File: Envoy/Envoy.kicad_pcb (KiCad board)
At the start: 2 copper layers, 95.4 x 95.4 mm, 57 parts

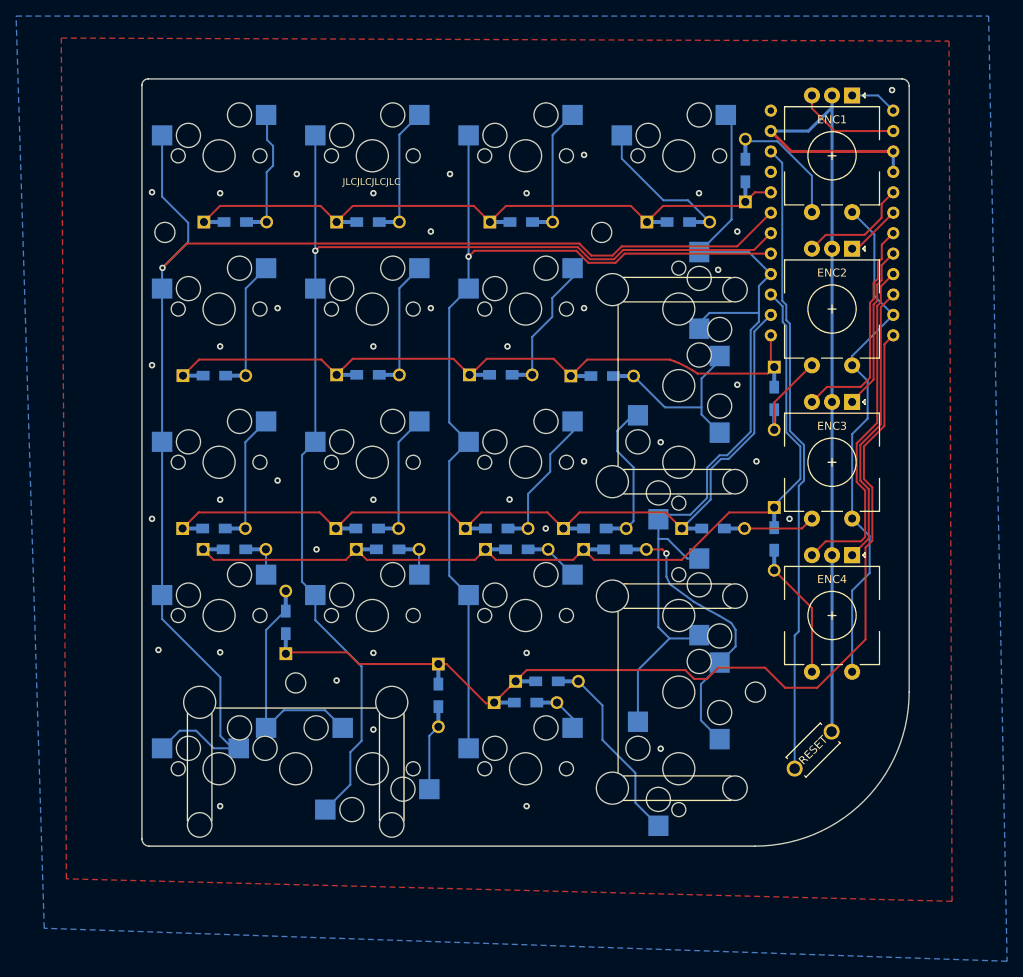
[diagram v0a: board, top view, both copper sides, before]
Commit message: curves!  Fun curved traces.  Prepare rev0.2 gerbers
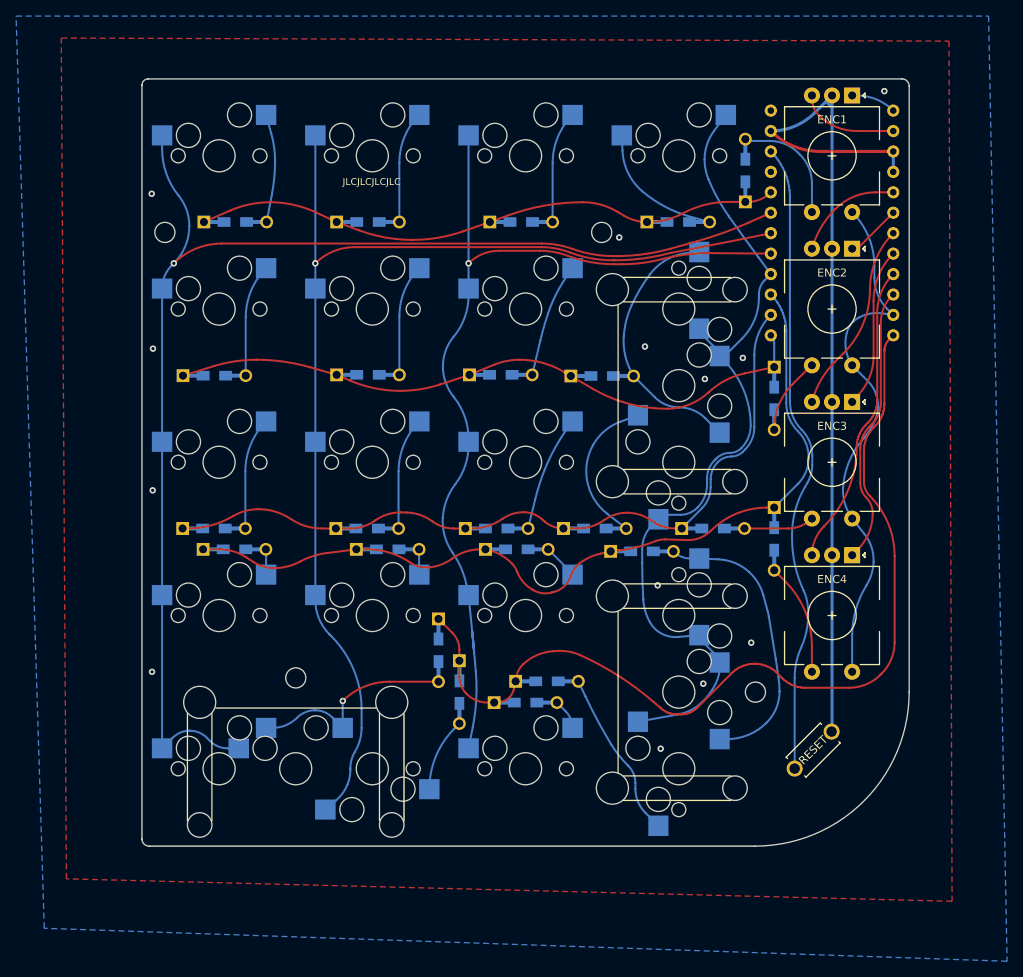
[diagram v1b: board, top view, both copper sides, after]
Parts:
- MX16, MX8: footprint Envoy:MXOnly-1U-Hotswap-2KeyAlternativeLeft -> Envoy:MXOnly-1U-HotswapReversed-2KeyAlternativeLeft
- moved D17 19.3 mm to (136.9, 126.5), turned to 90 degrees
- moved D16 3.37 mm to (162.2, 114.2)
- moved D18 2.64 mm to (139.5, 131.7)
- moved H3 0.63 mm to (119.1, 130.0)
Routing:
- net Net-(D8-Pad2): track 21.5 -> 33.8 mm
- net col0: track 173.6 -> 163.7 mm
- net col3: track 114.1 -> 106.9 mm
- net row4: track 121.2 -> 115.4 mm
- net enc4B: track 42.6 -> 37.6 mm
- net col1: track 148.2 -> 143.7 mm
- net row2: track 100.4 -> 96.5 mm
- net enc3B: track 27.6 -> 23.8 mm
- net row0: track 77.0 -> 73.5 mm
- net col2: track 119.2 -> 122.4 mm
- net Net-(D12-Pad2): track 16.1 -> 19.3 mm
- net row1: track 84.2 -> 81.4 mm
- net Net-(D16-Pad2): track 33.0 -> 35.3 mm, vias 1 -> 0
- net col4: track 64.8 -> 67.0 mm
- net Net-(D20-Pad2): track 22.1 -> 21.0 mm
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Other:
- rule pad_to_mask_clearance: 0.05 -> 0

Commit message: Moved a standoff hole and the feet.  Bumped pcb revision to 1.0
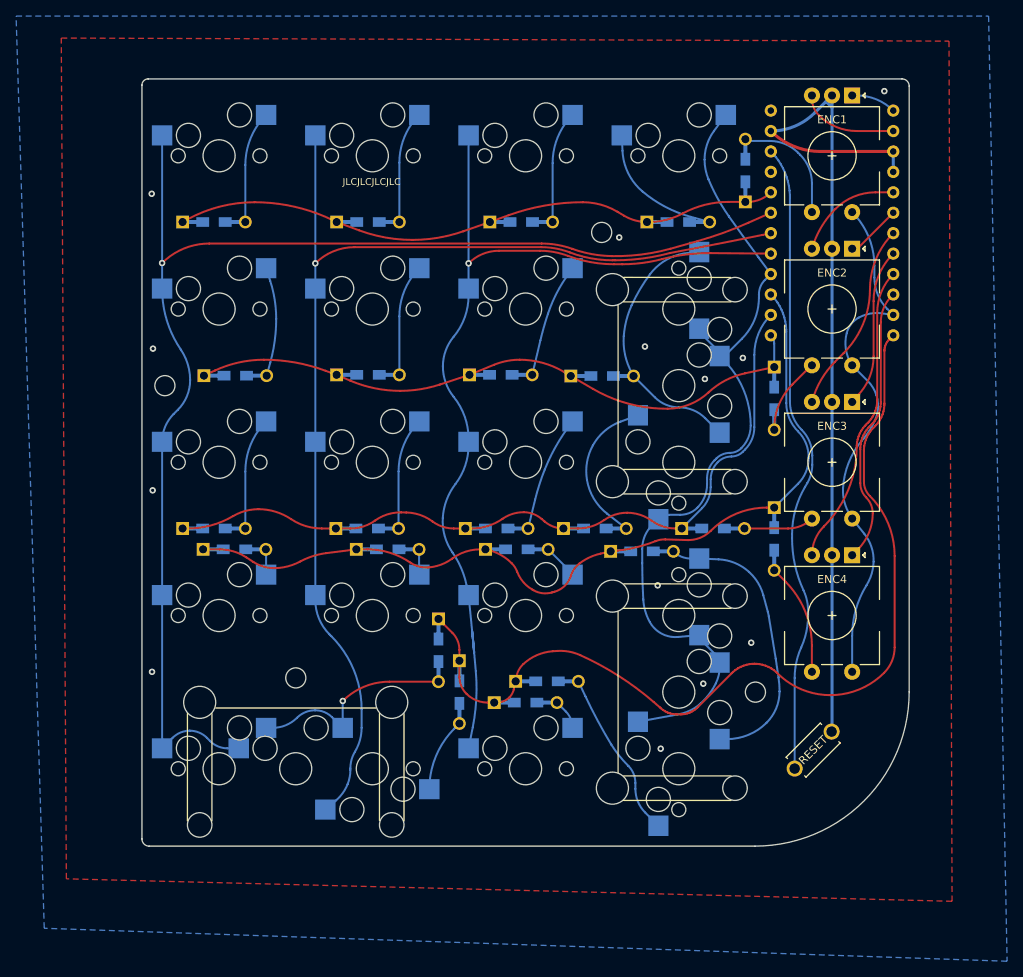
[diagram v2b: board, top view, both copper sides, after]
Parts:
- moved H1 19.0 mm to (102.9, 93.6)
- moved D1 2.65 mm to (109.0, 73.3)
- moved D5 2.60 mm to (111.6, 92.4)
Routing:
- net row0: track 73.5 -> 76.0 mm
- net row1: track 81.4 -> 78.9 mm
- net col0: track 163.7 -> 166.1 mm
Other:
- board text added: "Envoy by JeJeff rev 1.0"
- board text removed: "Envoy by JeJeff rev 0.2"
